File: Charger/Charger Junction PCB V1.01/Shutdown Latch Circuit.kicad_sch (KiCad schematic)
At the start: 16 parts, among them Q202 A03400A, U1 CD4043, U202 NE555D

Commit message: Added footprints
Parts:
- C1: footprint (none) -> Capacitor_SMD:C_0805_2012Metric_Pad1.18x1.45mm_HandSolder
- U1: value CD4043 -> CD4043B; Distributor Digikey -> (none); Height (mm) 1.2 -> (none); Length (mm) 5 -> (none); MPN CD4043BPWR -> (none); Max Power (W) 0.5 -> (none); Nominal Power (W) 0.12 -> (none); Operating Voltage (V) 12 -> (none); Package Type SMD -> (none); Price 0.82 -> (none); Purpose Shutdown Latches -> (none); Quantity 1 -> (none); URL https://www.digikey.com/short/3m54t2h2 -> (none); Width (mm) 6.4 -> (none)

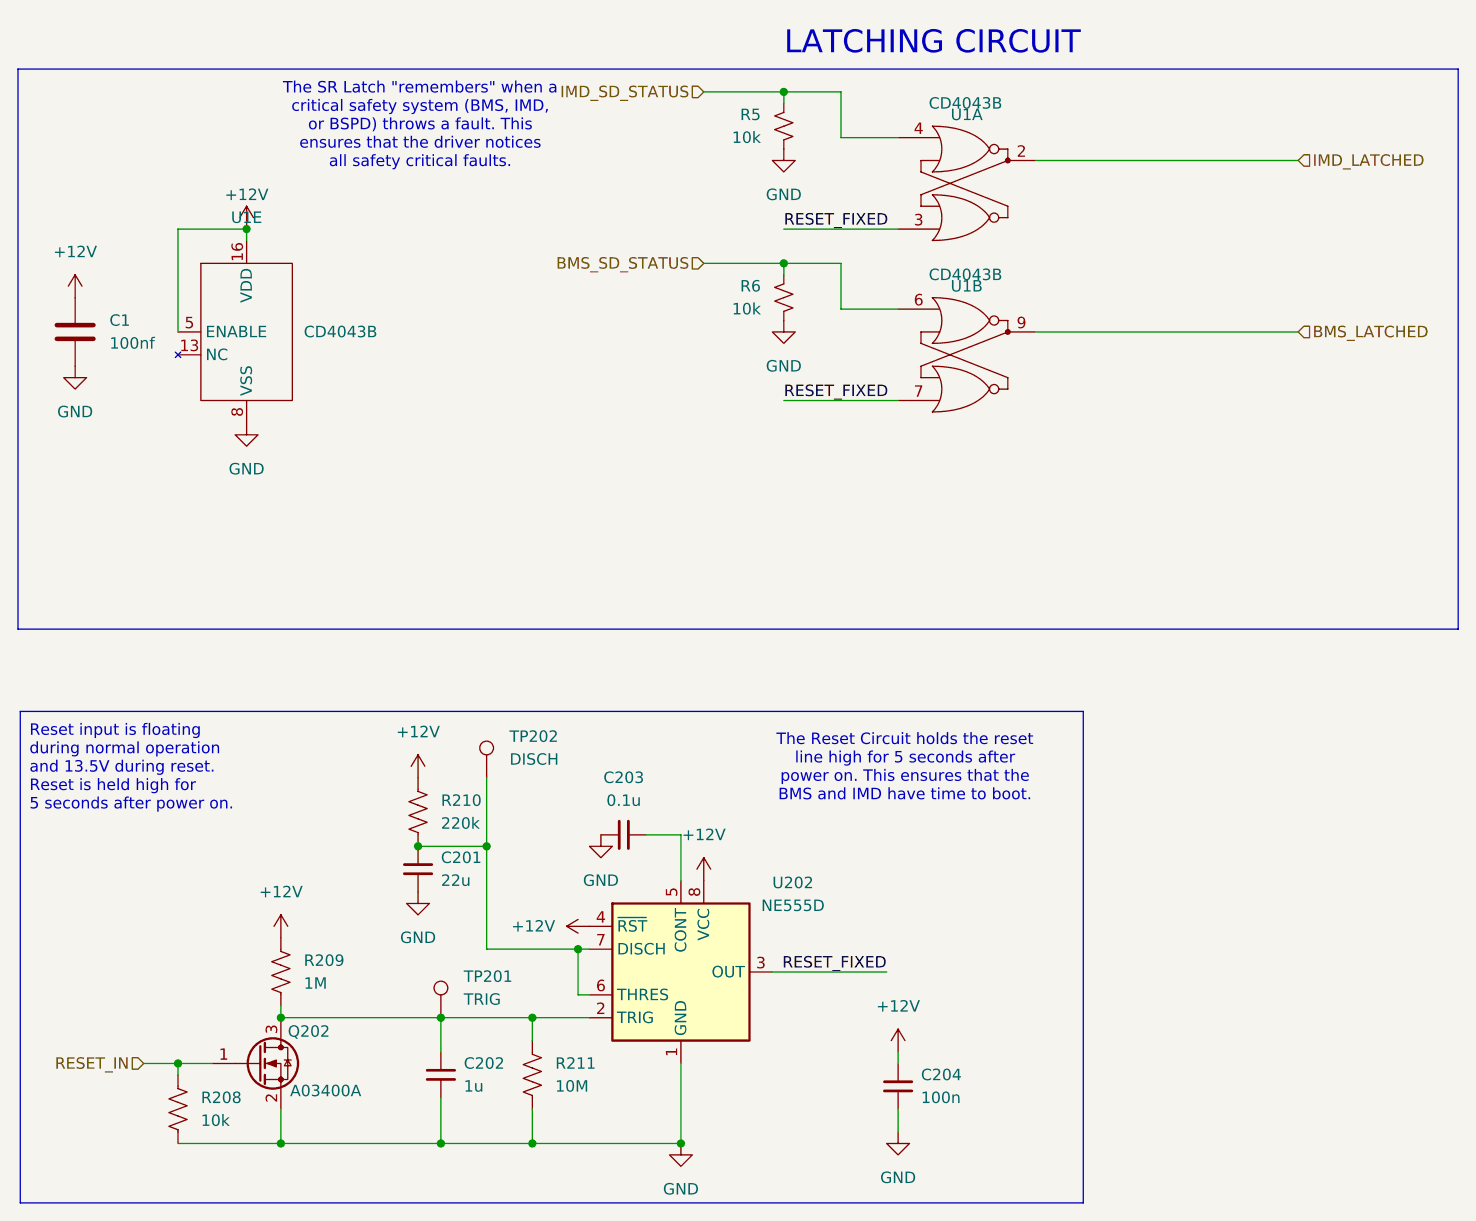
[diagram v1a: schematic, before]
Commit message: Added TVS diodes, fixed symbols and footprints
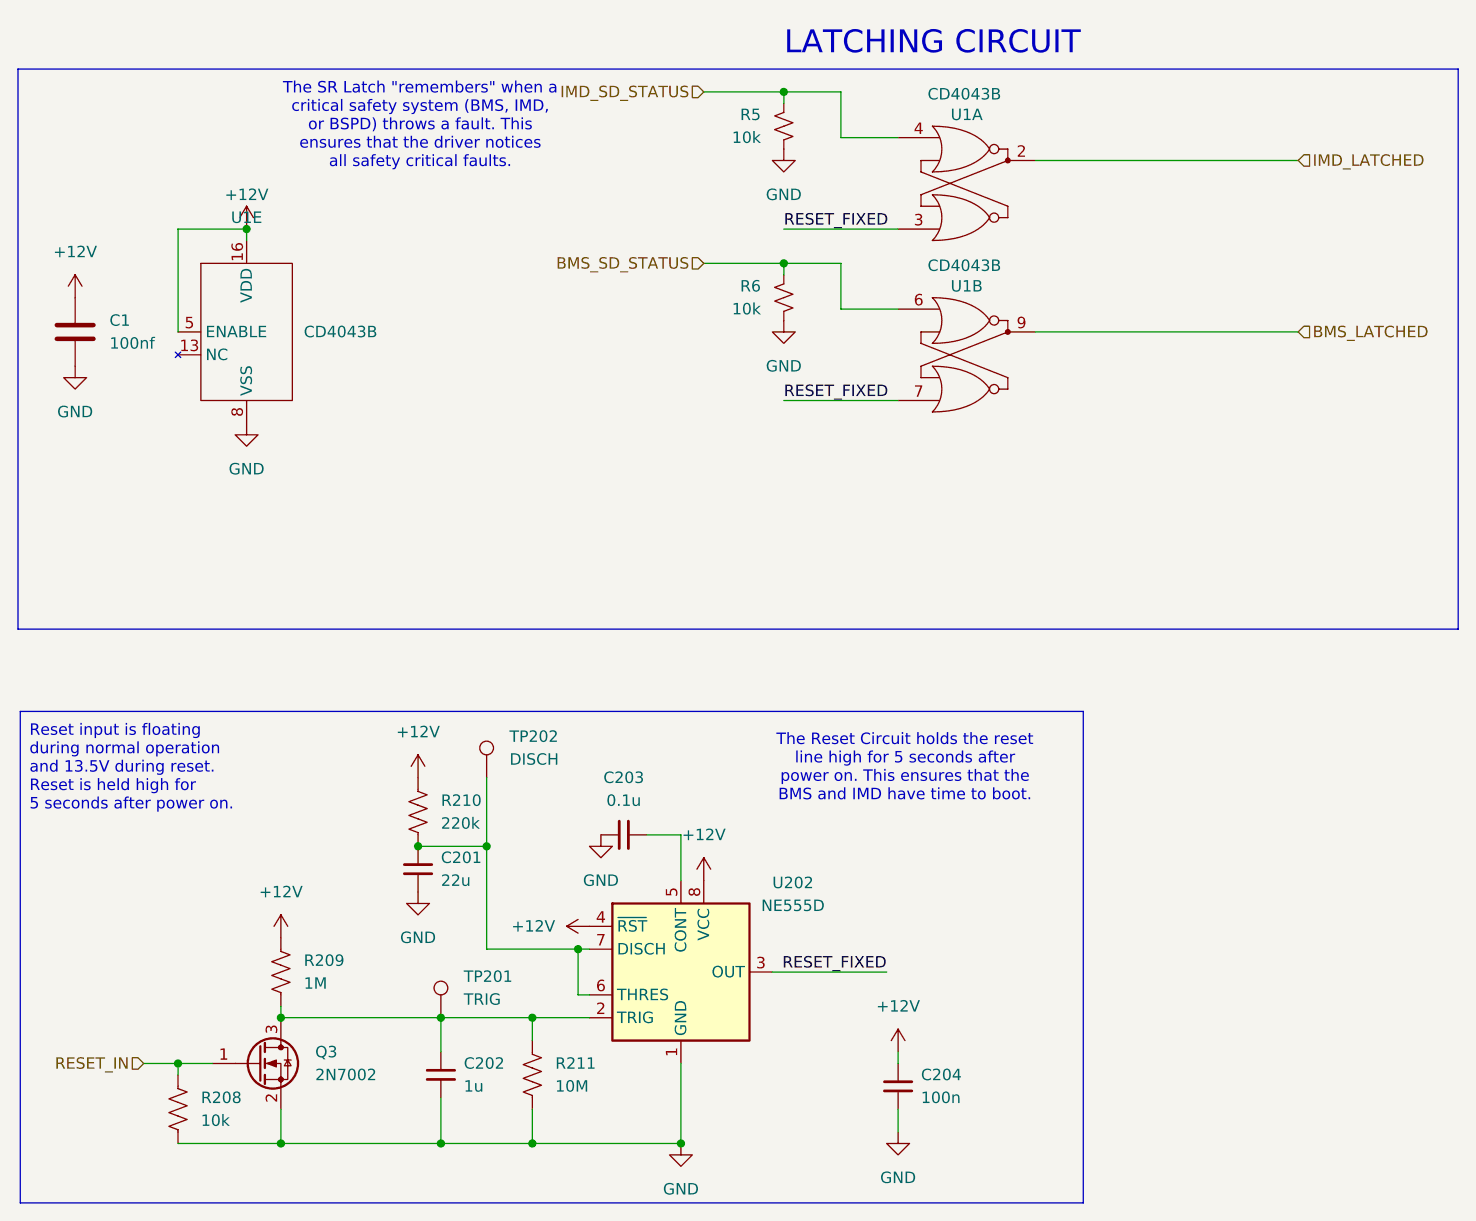
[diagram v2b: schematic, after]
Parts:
- removed Q202: A03400A, Package_TO_SOT_SMD:SOT-23_Handsoldering, symbol Transistor_FET:Q_NMOS_GSD
- added Q3: 2N7002, Package_TO_SOT_SMD:SOT-23, symbol Transistor_FET:2N7002
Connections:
- net GND: now also Q3.2 (S)
- net RESET_IN: now also Q3.1 (G)
- net at C202.2, R209.1, R211.2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: now also Q3.3 (D)
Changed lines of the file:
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@@
-	)
-	(junction
-		(at 59.69 132.08)
-		(diameter 0)
-		(color 0 0 0 0)
 	)
 	(junction
@@
 	(junction
 		(at 48.26 137.16)
+		(diameter 0)
+		(color 0 0 0 0)
+	)
+	(junction
+		(at 59.69 132.08)
 		(diameter 0)
 		(color 0 0 0 0)
@@
 				(path "/75f6fa4d-fba8-4d29-9299-863888d8bb95/ff12ffa7-fa4b-4c9b-853c-6398452d650b"
 					(reference "#PWR014")
+					(unit 1)
+				)
+			)
+		)
+	)
+	(symbol
+		(lib_id "Transistor_FET:2N7002")
+		(at 57.15 137.16 0)
+		(unit 1)
+		(body_style 1)
+		(exclude_from_sim no)
+		(in_bom yes)
+		(on_board yes)
+		(in_pos_files yes)
+		(dnp no)
+		(fields_autoplaced yes)
+		(property "Reference" "Q3"
+			(at 63.5 135.8899 0)
+			(show_name no)
+			(do_not_autoplace no)
+			(effects
+				(font
+					(size 1.27 1.27)
+				)
+				(justify left)
+			)
+		)
+		(property "Value" "2N7002"
+			(at 63.5 138.4299 0)
+			(show_name no)
+			(do_not_autoplace no)
+			(effects
+				(font
+					(size 1.27 1.27)
+				)
+				(justify left)
+			)
+		)
+		(property "Footprint" "Package_TO_SOT_SMD:SOT-23"
+			(at 62.23 139.065 0)
+			(hide yes)
+			(show_name no)
+			(do_not_autoplace no)
+			(effects
+				(font
+					(size 1.27 1.27)
+					(italic yes)
+				)
+				(justify left)
+			)
+		)
+		(property "Datasheet" "https://www.onsemi.com/pub/Collateral/NDS7002A-D.PDF"
+			(at 62.23 140.97 0)
+			(hide yes)
+			(show_name no)
+			(do_not_autoplace no)
+			(effects
+				(font
+					(size 1.27 1.27)
+				)
+				(justify left)
+			)
+		)
+		(property "Description" "0.115A Id, 60V Vds, N-Channel MOSFET, SOT-23"
+			(at 57.15 137.16 0)
+			(hide yes)
+			(show_name no)
+			(do_not_autoplace no)
+			(effects
+				(font
+					(size 1.27 1.27)
+				)
+			)
+		)
+		(pin "3"
+		)
+		(pin "2"
+		)
+		(pin "1"
+		)
+		(instances
+			(project "Charger Junction PCB V1.01"
+				(path "/75f6fa4d-fba8-4d29-9299-863888d8bb95/ff12ffa7-fa4b-4c9b-853c-6398452d650b"
+					(reference "Q3")
 					(unit 1)
 				)
@@
 		(in_pos_files yes)
 		(dnp no)
-		(fields_autoplaced yes)
 		(property "Reference" "U1"
 			(at 135.89 31.75 0)
@@
 		)
 		(property "Value" "CD4043B"
-			(at 135.763 30.48 0)
+			(at 135.636 29.464 0)
 			(show_name no)
 			(do_not_autoplace no)
@@
 	)
 	(symbol
-		(lib_id "Transistor_FET:Q_NMOS_GSD")
-		(at 57.15 137.16 0)
-		(unit 1)
-		(body_style 1)
-		(exclude_from_sim no)
-		(in_bom yes)
-		(on_board yes)
-		(in_pos_files yes)
-		(dnp no)
-		(property "Reference" "Q202"
-			(at 60.452 133.604 0)
-			(show_name no)
-			(do_not_autoplace no)
-			(effects
-				(font
-					(size 1.27 1.27)
-				)
-				(justify left)
-			)
-		)
-		(property "Value" "A03400A"
-			(at 60.706 140.208 0)
-			(show_name no)
-			(do_not_autoplace no)
-			(effects
-				(font
-					(size 1.27 1.27)
-				)
-				(justify left)
-			)
-		)
-		(property "Footprint" "Package_TO_SOT_SMD:SOT-23_Handsoldering"
-			(at 62.23 134.62 0)
-			(hide yes)
-			(show_name no)
-			(do_not_autoplace no)
-			(effects
-				(font
-					(size 1.27 1.27)
-				)
-			)
-		)
-		(property "Datasheet" "https://assets.nexperia.com/documents/data-sheet/BSS138P.pdf"
-			(at 57.15 137.16 0)
-			(hide yes)
-			(show_name no)
-			(do_not_autoplace no)
-			(effects
-				(font
-					(size 1.27 1.27)
-				)
-			)
-		)
-		(property "Description" "N-MOSFET transistor, gate/source/drain"
-			(at 57.15 137.16 0)
-			(hide yes)
-			(show_name no)
-			(do_not_autoplace no)
-			(effects
-				(font
-					(size 1.27 1.27)
-				)
-			)
-		)
-		(property "Distributor" "Digikey"
-			(at 57.15 137.16 0)
-			(hide yes)
-			(show_name no)
-			(do_not_autoplace no)
-			(effects
-				(font
-					(size 1.27 1.27)
-				)
-			)
-		)
-		(property "Height (mm)" "1.1"
-			(at 57.15 137.16 0)
-			(hide yes)
-			(show_name no)
-			(do_not_autoplace no)
-			(effects
-				(font
-					(size 1.27 1.27)
-				)
-			)
-		)
-		(property "Length (mm)" "3"
-			(at 57.15 137.16 0)
-			(hide yes)
-			(show_name no)
-			(do_not_autoplace no)
-			(effects
-				(font
-					(size 1.27 1.27)
-				)
-			)
-		)
-		(property "MPN" "BSS138P,215"
-			(at 57.15 137.16 0)
-			(hide yes)
-			(show_name no)
-			(do_not_autoplace no)
-			(effects
-				(font
-					(size 1.27 1.27)
-				)
-			)
-		)
-		(property "Max Power (W)" ".35"
-			(at 57.15 137.16 0)
-			(hide yes)
-			(show_name no)
-			(do_not_autoplace no)
-			(effects
-				(font
-					(size 1.27 1.27)
-				)
-			)
-		)
-		(property "Nominal Power (W)" ""
-			(at 57.15 137.16 0)
-			(hide yes)
-			(show_name no)
-			(do_not_autoplace no)
-			(effects
-				(font
-					(size 1.27 1.27)
-				)
-			)
-		)
-		(property "Operating Voltage (V)" ""
-			(at 57.15 137.16 0)
-			(hide yes)
-			(show_name no)
-			(do_not_autoplace no)
-			(effects
-				(font
-					(size 1.27 1.27)
-				)
-			)
-		)
-		(property "Package Type" "SOT-23"
-			(at 57.15 137.16 0)
-			(hide yes)
-			(show_name no)
-			(do_not_autoplace no)
-			(effects
-				(font
-					(size 1.27 1.27)
-				)
-			)
-		)
-		(property "Purpose" ""
-			(at 57.15 137.16 0)
-			(hide yes)
-			(show_name no)
-			(do_not_autoplace no)
-			(effects
-				(font
-					(size 1.27 1.27)
-				)
-			)
-		)
-		(property "Quantity" "1"
-			(at 57.15 137.16 0)
-			(hide yes)
-			(show_name no)
-			(do_not_autoplace no)
-			(effects
-				(font
-					(size 1.27 1.27)
-				)
-			)
-		)
-		(property "URL" "https://www.digikey.com/en/products/detail/nexperia-usa-inc/BSS138P-215/2779827"
-			(at 57.15 137.16 0)
-			(hide yes)
-			(show_name no)
-			(do_not_autoplace no)
-			(effects
-				(font
-					(size 1.27 1.27)
-				)
-			)
-		)
-		(property "Width (mm)" "2.5"
-			(at 57.15 137.16 0)
-			(hide yes)
-			(show_name no)
-			(do_not_autoplace no)
-			(effects
-				(font
-					(size 1.27 1.27)
-				)
-			)
-		)
-		(property "Description_1" ""
-			(at 57.15 137.16 0)
-			(hide yes)
-			(show_name no)
-			(do_not_autoplace no)
-			(effects
-				(font
-					(size 1.27 1.27)
-				)
-			)
-		)
-		(property "Price" "0.21"
-			(at 57.15 137.16 0)
-			(hide yes)
-			(show_name no)
-			(do_not_autoplace no)
-			(effects
-				(font
-					(size 1.27 1.27)
-				)
-			)
-		)
-		(pin "1"
-		)
-		(pin "2"
-		)
-		(pin "3"
-		)
-		(instances
-			(project "Charger Junction PCB V1.01"
-				(path "/75f6fa4d-fba8-4d29-9299-863888d8bb95/ff12ffa7-fa4b-4c9b-853c-6398452d650b"
-					(reference "Q202")
-					(unit 1)
-				)
-			)
-		)
-	)
-	(symbol
 		(lib_id "Device:R_Small_US")
 		(at 115.57 33.02 0)
@@
 		(in_pos_files yes)
 		(dnp no)
-		(fields_autoplaced yes)
 		(property "Reference" "U1"
 			(at 135.89 50.8 0)
@@
 		)
 		(property "Value" "CD4043B"
-			(at 135.763 49.53 0)
-			(show_name no)
-			(do_not_autoplace no)
+			(at 135.636 48.514 0)
+			(show_name no)
+			(do_not_autoplace no)
